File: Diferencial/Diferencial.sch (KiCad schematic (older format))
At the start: 68 parts, among them J1 Pedal Sensor 1, J2 Pedal Sensor 2, J3 DB9_Female, J4 DB9_Female, J5 Screw_Terminal_01x02, J6 Brake Sensor, J7 Out_Brake_Light, K1 RELAY_19.1x15.5mm, Q1 BC547, Q2 BC547, U1 LM358, U2 LM358, U3 MCP2558FD-xSN, U4 LM317_TO39, U5 UFRGS_PILL

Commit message: Diferencial Update
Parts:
- added C14: 100n, Capacitor_SMD:C_0805_2012Metric_Pad1.15x1.40mm_HandSolder, symbol Device:C
- added C15: 1u, Capacitor_SMD:C_0805_2012Metric_Pad1.15x1.40mm_HandSolder, symbol Device:C
- added D7: LED, e-Power:LED_0805_1.15x1.40mm_HandSolder, symbol Device:LED
- added J8: Brake Sensor 2, Connector_Phoenix_GMSTB:PhoenixContact_GMSTBA_2,5_3-G_1x03_P7.50mm_Horizontal, symbol Connector_Generic:Conn_01x03
- added R33, R36: ADJ, Resistor_SMD:R_0805_2012Metric_Pad1.15x1.40mm_HandSolder, symbol Device:R
- added R34: 2K7, Resistor_SMD:R_0805_2012Metric_Pad1.15x1.40mm_HandSolder, symbol Device:R
- added R35: 2K2, Resistor_SMD:R_0805_2012Metric_Pad1.15x1.40mm_HandSolder, symbol Device:R
- added R37: 3K3, Resistor_SMD:R_0805_2012Metric_Pad1.15x1.40mm_HandSolder, symbol Device:R
- added R38, R39, R40: 10K, Resistor_SMD:R_0805_2012Metric_Pad1.15x1.40mm_HandSolder, symbol Device:R
- added R41: 330, Resistor_SMD:R_0805_2012Metric_Pad1.15x1.40mm_HandSolder, symbol Device:R
- added unit 2 of U2
- J6: value Brake Sensor -> Brake Sensor 1
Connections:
- net labels added: Brake_Sensor_1, Brake_Sensor_2
- net labels removed: Brake_Sensor, PA5, PA6, PA7, Steering_Wheel
- wire segments 130 -> 160
- no-connect marks 30 -> 29
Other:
- note added: "Acceleration Pedal"
- note added: "Brake Light Signal"
- note added: "Brake Pedal"
- note added: "CAN"
- note added: "Input Filter"
- note added: "Ready to Drive"
- moved on the sheet: C10, C11, C12, C13, C2, C3, C5, C6, C7, C8, C9, D2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

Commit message: Diferencial Layout Update/Main ECU Eeschema
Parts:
- removed D1: D_SCH_1N5819, Diode_SMD:D_SOD-323_HandSoldering, symbol e-Power:D_SCH_1N5819
- removed D5: 1N4148, e-Power:DO-35_SMD, symbol Diode:1N4148
- removed Q1: BC547, Package_TO_SOT_SMD:SC-59_Handsoldering, symbol Transistor_BJT:BC547
- removed Q2: BC547, e-Power:SOT-23, symbol Transistor_BJT:BC547
- removed R10, R36: ADJ, Resistor_SMD:R_0805_2012Metric_Pad1.15x1.40mm_HandSolder, symbol Device:R
- removed R11: 2K2, Resistor_SMD:R_0805_2012Metric_Pad1.15x1.40mm_HandSolder, symbol Device:R
- removed R2: 1K2, Resistor_SMD:R_0805_2012Metric_Pad1.15x1.40mm_HandSolder, symbol Device:R
- removed R22, R23, R24: 330, Resistor_SMD:R_0805_2012Metric_Pad1.15x1.40mm_HandSolder, symbol Device:R
- removed R34: 2K7, Resistor_SMD:R_0805_2012Metric_Pad1.15x1.40mm_HandSolder, symbol Device:R
- added D5, D6: D_SCH_SS54HF, e-Power:DO-214AC, symbol e-Power:D_SCH_SS54HF
- added G1: Logo_UFRGS_Large, e-Power:Logo_UFRGS_14.7x8.0mm_SilkS, symbol e-Power:Logo_UFRGS_Large
- added G2: Logo_e-Power_Large, e-Power:Logo_e-Power_16.5x8.0mm_SilkS, symbol e-Power:Logo_e-Power_Large
- added H1: +12V, e-Power:MountingHole_3.2mm_M3_Pad_Via, symbol Mechanical:MountingHole_Pad
- added H2, H3, H4: GND, e-Power:MountingHole_3.2mm_M3_Pad_Via, symbol Mechanical:MountingHole_Pad
- added Q1, Q2: MMBT3904, Package_TO_SOT_SMD:SOT-23, symbol Transistor_BJT:MMBT3904
- added R15, R20, R31, R32, R43, R44, R50, R51, R52, R57, R8: 1K, Resistor_SMD:R_0805_2012Metric_Pad1.15x1.40mm_HandSolder, symbol Device:R
- added R16, R17, R26, R27, R29, R38, R39, R4, R40, R41, R7: 10K, Resistor_SMD:R_0805_2012Metric_Pad1.15x1.40mm_HandSolder, symbol Device:R
- added R46, R48: 10R, Resistor_SMD:R_0805_2012Metric_Pad1.15x1.40mm_HandSolder, symbol Device:R
- added TP1: 12V, e-Power:TestPoint_Pad_D1.0mm, symbol Connector:TestPoint
- added TP2: 5V, e-Power:TestPoint_Pad_D1.0mm, symbol Connector:TestPoint
- added TP? (x7): GND, e-Power:TestPoint_Pad_D1.0mm, symbol Connector:TestPoint
- C14: renamed from C12; value 470u -> 220u
- C15: renamed from C13; value 470u -> 220u
- F1: footprint Fuse:Fuse_0805_2012Metric_Pad1.15x1.40mm_HandSolder -> e-Power:FUSE_1206_3216Metric
- FB1: footprint e-Power:FB_0603_1608Metric -> e-Power:FB_0805_2012Metric
- J1, J2: footprint Connector_Phoenix_GMSTB:PhoenixContact_GMSTBA_2,5_3-G_1x03_P7.50mm_Horizontal -> e-Power:TerminalBlock_Phoenix_MKDS-1,5-4-5.08_1x04_P5.08mm_Horizontal
- J3: renamed from J6; footprint Connector_Phoenix_GMSTB:PhoenixContact_GMSTBA_2,5_3-G_1x03_P7.50mm_Horizontal -> e-Power:TerminalBlock_Phoenix_MKDS-1,5-4-5.08_1x04_P5.08mm_Horizontal
- J4: renamed from J8; footprint Connector_Phoenix_GMSTB:PhoenixContact_GMSTBA_2,5_3-G_1x03_P7.50mm_Horizontal -> e-Power:TerminalBlock_Phoenix_MKDS-1,5-4-5.08_1x04_P5.08mm_Horizontal
- J5: renamed from J7; footprint Connector_Phoenix_GMSTB:PhoenixContact_GMSTBA_2,5_2-G-7,62_1x02_P7.62mm_Horizontal -> e-Power:TerminalBlock_Phoenix_MKDS-1,5-2_1x02_P5.08mm_Horizontal
- J6: renamed from J5; value Screw_Terminal_01x02 -> Buzzer_out; footprint Connector_Phoenix_GMSTB:PhoenixContact_GMSTBA_2,5_2-G-7,62_1x02_P7.62mm_Horizontal -> e-Power:TerminalBlock_Phoenix_MKDS-1,5-2_1x02_P5.08mm_Horizontal
- R13, R28: value 2K2 -> 10K
- R14, R21: value 330 -> 1K
- R18: value 2K7 -> 1K
- R22: renamed from R41; value 330 -> 1K
- R3: value 18K -> ADJ
- R30, R37: value 3K3 -> 10K
- R35: value 2K2 -> ADJ
- R49: renamed from R19; value 120 -> 100R
- R5: value 1K2 -> 1K
- R6: value 18K -> 10K
- U1: footprint e-Power:DIP-8_SMD -> Package_SO:SOIC-8_3.9x4.9mm_P1.27mm
- U3: renamed from U2; footprint e-Power:DIP-8_SMD -> Package_SO:SOIC-8_3.9x4.9mm_P1.27mm
- U5: renamed from U4; footprint Package_TO_SOT_THT:TO-39-3 -> e-Power:TO-220-3_Horizontal_TabDown
- renumbered C15 to C10, C10 to C11, C9 to C12, C11 to C13, C4 to C2, C7 to C3, C2 to C4, C3 to C6, C6 to C7, C14 to C9, D2 to D1, D3 to D2, D4 to D3, D7 to D4, D6 to D7, J3 to J7, J4 to J8, R17 to R10, R12 to R11, R7 to R12, R8 to R19, R16 to R2, R15 to R23, R31 to R24, R29 to R25, R38 to R34, R39 to R36, R40 to R42, R32 to R45, R20 to R47, R26 to R53, R25 to R54, R27 to R55, R9 to R56, R4 to R9, U5 to U2, U2 to U3, U3 to U4
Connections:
- wire segments 160 -> 202
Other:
- moved on the sheet: J1, J2, J3, J4, R23, R25, R49, R53, R9

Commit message: Diferencial Layout Update
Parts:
- removed J7: DB9_Female, e-Power:DSUB-9_Female_EdgeMount_P2.77mm, symbol Connector:DB9_Female
- removed U5: LM317_TO39, e-Power:TO-220-3_Horizontal_TabDown, symbol Regulator_Linear:LM317_TO39
- added J7: Screw_Terminal_01x04, e-Power:TerminalBlock_Phoenix_MKDS-1,5-4-5.08_1x04_P5.08mm_Horizontal, symbol Connector:Screw_Terminal_01x04
- added U5: LM317_3PinPackage, e-Power:TO-220-3_Horizontal_TabDown, symbol Regulator_Linear:LM317_3PinPackage
- TP3: renamed from TP?; value GND -> AS_1
- TP4: renamed from TP?; value GND -> AS_2
- TP6: renamed from TP?; value GND -> BS_1
- TP7: renamed from TP?; value GND -> BS_2
- gave numbers to parts that had none: 3
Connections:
- net +12V: now also U5.3 (VI)
- net +5V: now also U5.2 (VO)
- net Brake_Light: now also U2.25 (PA1); no longer U2.10 (PA9)
- net Brake_Sensor_1: now also U2.10 (PA9); no longer U2.25 (PA1)
- net Brake_Sensor_2: now also U2.9 (PA8); no longer U2.24 (PA0)
- net CAN_H: now also J7.3 (Pin_3)
- net CAN_L: now also J7.2 (Pin_2)
- net GND: now also J7.1 (Pin_1)
- net Input_Power: now also J7.4 (Pin_4)
- net Ready_to_Drive: now also U2.24 (PA0); no longer U2.9 (PA8)
- net at R50.2, R51.2, R52.2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: now also U5.1 (ADJ)
- no-connect marks 29 -> 27
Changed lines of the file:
@@
-	1    0    0    -1
-$EndComp
-$Comp
-L Regulator_Linear:LM317_TO39 U5
-U 1 1 5ECB47C0
-P 14475 8525
-F 0 "U5" H 14475 8767 50  0000 C CNN
-F 1 "LM317_TO39" H 14475 8676 50  0000 C CNN
-F 2 "e-Power:TO-220-3_Horizontal_TabDown" H 14475 8750 50  0001 C CIN
-F 3 "http://www.ti.com/lit/ds/symlink/lm317.pdf" H 14475 8525 50  0001 C CNN
-	1    14475 8525
 	1    0    0    -1
 $EndComp
@@
 	1    0    0    -1
 $EndComp
-$Comp
-L Connector:DB9_Female J7
-U 1 1 5ED2A193
-P 1550 9900
-F 0 "J7" H 1730 9946 50  0000 L CNN
-F 1 "DB9_Female" H 1730 9855 50  0000 L CNN
-F 2 "e-Power:DSUB-9_Female_EdgeMount_P2.77mm" H 1550 9900 50  0001 C CNN
-F 3 " ~" H 1550 9900 50  0001 C CNN
-	1    1550 9900
-	-1   0    0    1
-$EndComp
-$Comp
-L power:GND #PWR054
-U 1 1 5ED2A199
-P 1850 10200
-F 0 "#PWR054" H 1850 9950 50  0001 C CNN
-F 1 "GND" V 1855 10072 50  0000 R CNN
-F 2 "" H 1850 10200 50  0001 C CNN
-F 3 "" H 1850 10200 50  0001 C CNN
-	1    1850 10200
-	0    -1   -1   0
-$EndComp
-$Comp
-L power:GND #PWR048
-U 1 1 5ED2A19F
-P 1850 9500
-F 0 "#PWR048" H 1850 9250 50  0001 C CNN
-F 1 "GND" V 1855 9372 50  0000 R CNN
-F 2 "" H 1850 9500 50  0001 C CNN
-F 3 "" H 1850 9500 50  0001 C CNN
-	1    1850 9500
-	0    -1   -1   0
-$EndComp
-Wire Wire Line
-	1850 9600 2425 9600
-Text Label 2425 9600 2    50   ~ 0
+Wire Wire Line
+	1725 9775 2300 9775
+Text Label 2300 9775 2    50   ~ 0
+CAN_H
+Wire Wire Line
+	1725 9875 2300 9875
+Text Label 2300 9875 2    50   ~ 0
+CAN_L
+Wire Wire Line
+	1725 9975 2300 9975
+Text Label 2300 9975 2    50   ~ 0
+CAN_GND
+Wire Wire Line
+	1725 9675 2300 9675
+Text Label 2300 9675 2    50   ~ 0
 Input_Power
-Wire Wire Line
-	1850 10000 2425 10000
-Text Label 2425 10000 2    50   ~ 0
-CAN_H
-Wire Wire Line
-	1850 10100 2425 10100
-Text Label 2425 10100 2    50   ~ 0
-CAN_L
-Wire Wire Line
-	1850 9900 2425 9900
-Text Label 2425 9900 2    50   ~ 0
-CAN_GND
-Wire Wire Line
-	1850 10300 2425 10300
-Text Label 2425 10300 2    50   ~ 0
-Input_Power
-NoConn ~ 1850 9700
-NoConn ~ 1850 9800
-Text Label 10500 2925 2    50   ~ 0
+Text Label 11550 3725 0    50   ~ 0
 Ready_to_Drive
 Text Label 6475 9325 2    50   ~ 0
@@
 $EndComp
 NoConn ~ 8825 8500
-Text Label 11550 3625 0    50   ~ 0
+Text Label 10500 3025 2    50   ~ 0
 Brake_Sensor_1
 Connection ~ 4000 2450
@@
 	1    0    0    -1
 $EndComp
-Wire Wire Line
-	4925 4175 4950 4175
 Connection ~ 4925 4175
 $Comp
@@
 	-1   0    0    1
 $EndComp
-Text Label 5175 4175 0    50   ~ 0
-Brake_Sensor_1
 Connection ~ 4425 4175
 Wire Wire Line
@@
 Text Label 15125 7325 0    50   ~ 0
 Brake_Light
-Text Label 10500 3025 2    50   ~ 0
+Text Label 11550 3625 0    50   ~ 0
 Brake_Light
-Text Label 11550 3725 0    50   ~ 0
+Text Label 10500 2925 2    50   ~ 0
 Brake_Sensor_2
 Wire Notes Line
@@
 $EndComp
 $Comp
-L Connector:TestPoint TP?
+L Connector:TestPoint TP9
 U 1 1 5F3C7037
 P 14975 9450
-F 0 "TP?" H 14900 9725 50  0000 L CNN
+F 0 "TP9" H 14900 9725 50  0000 L CNN
 F 1 "GND" H 14900 9650 50  0000 L CNN
 F 2 "e-Power:TestPoint_Pad_D1.0mm" H 15175 9450 50  0001 C CNN
@@
 	14975 9450 14975 9500
 $Comp
-L Connector:TestPoint TP?
+L Connector:TestPoint TP3
 U 1 1 5F3C983B
 P 4925 1050
-F 0 "TP?" H 4850 1325 50  0000 L CNN
-F 1 "GND" H 4850 1250 50  0000 L CNN
+F 0 "TP3" H 4850 1325 50  0000 L CNN
+F 1 "AS_1" H 4850 1250 50  0000 L CNN
 F 2 "e-Power:TestPoint_Pad_D1.0mm" H 5125 1050 50  0001 C CNN
 F 3 "~" H 5125 1050 50  0001 C CNN
@@
 $EndComp
 $Comp
-L Connector:TestPoint TP?
+L Connector:TestPoint TP4
 U 1 1 5F3CA5F4
 P 4900 2450
-F 0 "TP?" H 4825 2725 50  0000 L CNN
-F 1 "GND" H 4825 2650 50  0000 L CNN
+F 0 "TP4" H 4825 2725 50  0000 L CNN
+F 1 "AS_2" H 4825 2650 50  0000 L CNN
 F 2 "e-Power:TestPoint_Pad_D1.0mm" H 5100 2450 50  0001 C CNN
 F 3 "~" H 5100 2450 50  0001 C CNN
@@
 $EndComp
 $Comp
-L Connector:TestPoint TP?
+L Connector:TestPoint TP7
 U 1 1 5F3CAABA
 P 4925 5675
-F 0 "TP?" H 4850 5950 50  0000 L CNN
-F 1 "GND" H 4850 5875 50  0000 L CNN
+F 0 "TP7" H 4850 5950 50  0000 L CNN
+F 1 "BS_2" H 4850 5875 50  0000 L CNN
 F 2 "e-Power:TestPoint_Pad_D1.0mm" H 5125 5675 50  0001 C CNN
 F 3 "~" H 5125 5675 50  0001 C CNN
@@
 	1    0    0    -1
 $EndComp
-Connection ~ 4950 4175
-Wire Wire Line
-	4950 4175 5175 4175
-$Comp
-L Connector:TestPoint TP?
+$Comp
+L Connector:TestPoint TP6
 U 1 1 5F3CB025
 P 4925 4175
-F 0 "TP?" H 4850 4450 50  0000 L CNN
-F 1 "GND" H 4850 4375 50  0000 L CNN
+F 0 "TP6" H 4850 4450 50  0000 L CNN
+F 1 "BS_1" H 4850 4375 50  0000 L CNN
 F 2 "e-Power:TestPoint_Pad_D1.0mm" H 5125 4175 50  0001 C CNN
 F 3 "~" H 5125 4175 50  0001 C CNN
@@
 $EndComp
 $Comp
-L Connector:TestPoint TP?
+L Connector:TestPoint TP8
 U 1 1 5F3CB6F0
 P 5475 6350
-F 0 "TP?" H 5400 6625 50  0000 L CNN
+F 0 "TP8" H 5400 6625 50  0000 L CNN
 F 1 "GND" H 5400 6550 50  0000 L CNN
 F 2 "e-Power:TestPoint_Pad_D1.0mm" H 5675 6350 50  0001 C CNN
@@
 $EndComp
 $Comp
-L Connector:TestPoint TP?
+L Connector:TestPoint TP5
 U 1 1 5F3CBF2E
 P 5475 3125
-F 0 "TP?" H 5400 3400 50  0000 L CNN
+F 0 "TP5" H 5400 3400 50  0000 L CNN
 F 1 "GND" H 5400 3325 50  0000 L CNN
 F 2 "e-Power:TestPoint_Pad_D1.0mm" H 5675 3125 50  0001 C CNN
@@
 Connection ~ 5475 3125
 Connection ~ 5475 6350
+Wire Wire Line
+	4925 4175 5175 4175
+$Comp
+L Regulator_Linear:LM317_3PinPackage U5
+U 1 1 5F3B31FD
+P 14475 8525
+F 0 "U5" H 14475 8767 50  0000 C CNN
+F 1 "LM317_3PinPackage" H 14475 8676 50  0000 C CNN
+F 2 "e-Power:TO-220-3_Horizontal_TabDown" H 14475 8775 50  0001 C CIN
+F 3 "http://www.ti.com/lit/ds/symlink/lm317.pdf" H 14475 8525 50  0001 C CNN
+	1    14475 8525
+	1    0    0    -1
+$EndComp
+Text Label 5175 4175 0    50   ~ 0
+Brake_Sensor_1
+$Comp
+L Connector:Screw_Terminal_01x04 J7
+U 1 1 5F83DA47
+P 1525 9875
+F 0 "J7" H 1443 9450 50  0000 C CNN
+F 1 "Screw_Terminal_01x04" H 1443 9541 50  0000 C CNN
+F 2 "e-Power:TerminalBlock_Phoenix_MKDS-1,5-4-5.08_1x04_P5.08mm_Horizontal" H 1525 9875 50  0001 C CNN
+F 3 "~" H 1525 9875 50  0001 C CNN
+	1    1525 9875
+	-1   0    0    1
+$EndComp
 $EndSCHEMATC

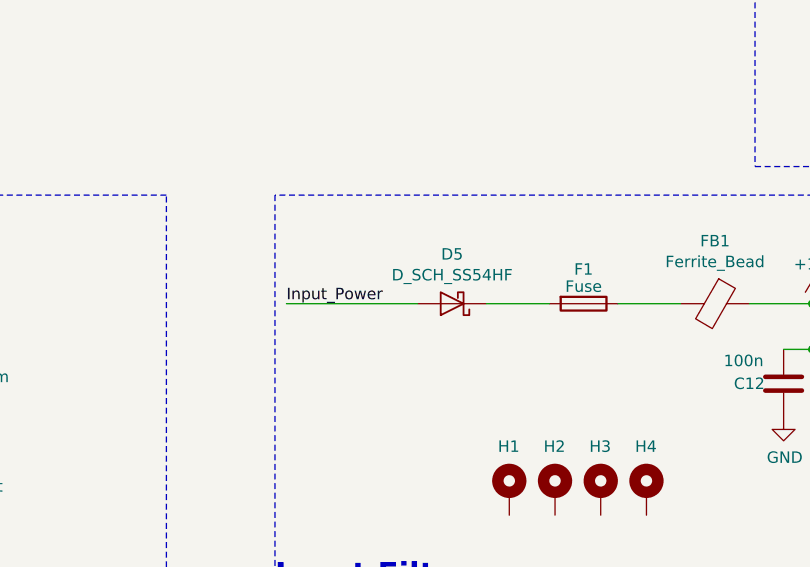
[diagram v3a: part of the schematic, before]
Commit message: Layout Fixes and CAN Connector Added
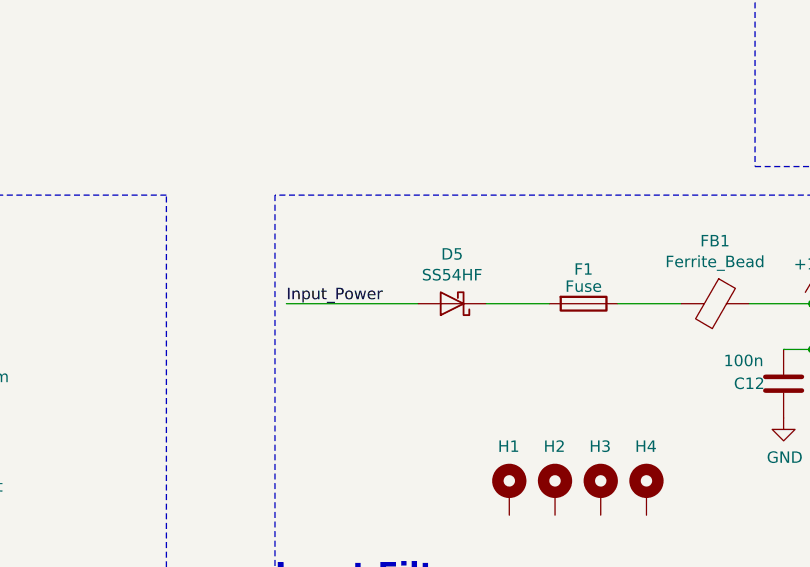
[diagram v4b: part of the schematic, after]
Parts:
- removed D5: D_SCH_SS54HF, e-Power:DO-214AC, symbol e-Power:D_SCH_SS54HF
- added D5: SS54HF, e-Power:DO-214AC, symbol e-Power:SS54HF
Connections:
- net Input_Power: now also D5.2 (A)
- net at F1.2: now also D5.1 (K)
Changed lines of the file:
@@
 NoConn ~ 4200 10100
 NoConn ~ 4200 10000
-Wire Wire Line
-	11675 8525 11100 8525
 Text Label 11100 8525 0    50   ~ 0
 Input_Power
@@
 	12850 2775 12850 3025
 $Comp
-L e-Power:D_SCH_SS54HF D5
-U 1 1 5F30CB96
-P 11825 8525
-F 0 "D5" H 11825 8309 50  0000 C CNN
-F 1 "D_SCH_SS54HF" H 11825 8400 50  0000 C CNN
-F 2 "e-Power:DO-214AC" H 11825 8350 50  0001 C CNN
-F 3 "https://br.mouser.com/datasheet/2/80/20190806165140-1729178.pdf" H 11700 8600 50  0001 C CNN
-F 4 "C22452" H 11825 8625 50  0001 C CNN "LCSC"
-	1    11825 8525
-	-1   0    0    1
-$EndComp
-$Comp
 L Connector:TestPoint TP1
 U 1 1 5F313597
@@
 	-1   0    0    1
 $EndComp
+$Comp
+L e-Power:SS54HF D5
+U 1 1 5F4E4A0E
+P 11825 8525
+F 0 "D5" H 11825 8309 50  0000 C CNN
+F 1 "SS54HF" H 11825 8400 50  0000 C CNN
+F 2 "e-Power:DO-214AC" H 11825 8350 50  0001 C CNN
+F 3 "" H 11825 8525 50  0001 C CNN
+	1    11825 8525
+	-1   0    0    1
+$EndComp
+Wire Wire Line
+	11100 8525 11675 8525
 $EndSCHEMATC

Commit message: Added CAN connectors / Fixes
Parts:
- removed J8: DB9_Female, e-Power:DSUB-9_Female_EdgeMount_P2.77mm, symbol Connector:DB9_Female
- removed R36, R42: 10K, Resistor_SMD:R_0805_2012Metric_Pad1.15x1.40mm_HandSolder, symbol Device:R
- removed TP8: GND, e-Power:TestPoint_Pad_D1.0mm, symbol Connector:TestPoint
- added J8: CAN_1, e-Power:Molex_Mini-Fit_Jr_2x04_P4.20mm_Horizontal, symbol Connector:Screw_Terminal_01x08
- C14, C15: footprint Capacitor_SMD:CP_Elec_8x10 -> Capacitor_SMD:CP_Elec_10x10
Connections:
- net Brake_Sensor_2: now also C10.2, C9.2, R34.2, TP7.1
- net CAN_H: now also J8.4 (Pin_4)
- net CAN_L: now also J8.3 (Pin_3)
- net GND: now also J8.2 (Pin_2), J8.5 (Pin_5), J8.8 (Pin_8)
- net Input_Power: now also J8.1 (Pin_1), J8.7 (Pin_7)
- no-connect marks 27 -> 26
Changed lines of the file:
@@
-$EndComp
-$Comp
-L Connector:DB9_Female J8
-U 1 1 5ECE338B
-P 4500 9900
-F 0 "J8" H 4680 9946 50  0000 L CNN
-F 1 "DB9_Female" H 4680 9855 50  0000 L CNN
-F 2 "e-Power:DSUB-9_Female_EdgeMount_P2.77mm" H 4500 9900 50  0001 C CNN
-F 3 " ~" H 4500 9900 50  0001 C CNN
-	1    4500 9900
-	1    0    0    -1
 $EndComp
 $Comp
 L power:GND #PWR051
 U 1 1 5ECE6E6B
-P 4200 9600
-F 0 "#PWR051" H 4200 9350 50  0001 C CNN
-F 1 "GND" V 4205 9472 50  0000 R CNN
-F 2 "" H 4200 9600 50  0001 C CNN
-F 3 "" H 4200 9600 50  0001 C CNN
-	1    4200 9600
+P 4675 9600
+F 0 "#PWR051" H 4675 9350 50  0001 C CNN
+F 1 "GND" V 4680 9472 50  0000 R CNN
+F 2 "" H 4675 9600 50  0001 C CNN
+F 3 "" H 4675 9600 50  0001 C CNN
+	1    4675 9600
 	0    1    1    0
 $EndComp
@@
 L power:GND #PWR055
 U 1 1 5ECE7C93
-P 4200 10300
-F 0 "#PWR055" H 4200 10050 50  0001 C CNN
-F 1 "GND" V 4205 10172 50  0000 R CNN
-F 2 "" H 4200 10300 50  0001 C CNN
-F 3 "" H 4200 10300 50  0001 C CNN
-	1    4200 10300
-	0    1    1    0
-$EndComp
-Wire Wire Line
-	4200 10200 3625 10200
-Text Label 3625 10200 0    50   ~ 0
+P 4675 10200
+F 0 "#PWR055" H 4675 9950 50  0001 C CNN
+F 1 "GND" V 4680 10072 50  0000 R CNN
+F 2 "" H 4675 10200 50  0001 C CNN
+F 3 "" H 4675 10200 50  0001 C CNN
+	1    4675 10200
+	0    1    1    0
+$EndComp
+Wire Wire Line
+	4675 10100 4100 10100
+Text Label 4100 10100 0    50   ~ 0
 Input_Power
 Wire Wire Line
-	4200 9800 3625 9800
-Text Label 3625 9800 0    50   ~ 0
+	4675 9800 4100 9800
+Text Label 4100 9800 0    50   ~ 0
 CAN_H
 Wire Wire Line
-	4200 9700 3625 9700
-Text Label 3625 9700 0    50   ~ 0
+	4675 9700 4100 9700
+Text Label 4100 9700 0    50   ~ 0
 CAN_L
 Wire Wire Line
-	4200 9900 3625 9900
-Text Label 3625 9900 0    50   ~ 0
+	4675 9900 4100 9900
+Text Label 4100 9900 0    50   ~ 0
 CAN_GND
 Wire Wire Line
-	4200 9500 3625 9500
-Text Label 3625 9500 0    50   ~ 0
+	4675 9500 4100 9500
+Text Label 4100 9500 0    50   ~ 0
 Input_Power
-NoConn ~ 4200 10100
-NoConn ~ 4200 10000
+NoConn ~ 4675 10000
 Text Label 11100 8525 0    50   ~ 0
 Input_Power
@@
 F 0 "C14" H 14100 8850 50  0000 L CNN
 F 1 "220u" H 14100 8925 50  0000 L CNN
-F 2 "Capacitor_SMD:CP_Elec_8x10" H 14038 8725 50  0001 C CNN
+F 2 "Capacitor_SMD:CP_Elec_10x10" H 14038 8725 50  0001 C CNN
 F 3 "~" H 14000 8875 50  0001 C CNN
 	1    14000 8875
@@
 F 0 "C15" H 15650 8825 50  0000 L CNN
 F 1 "220u" H 15650 8900 50  0000 L CNN
-F 2 "Capacitor_SMD:CP_Elec_8x10" H 15563 8725 50  0001 C CNN
+F 2 "Capacitor_SMD:CP_Elec_10x10" H 15563 8725 50  0001 C CNN
 F 3 "~" H 15525 8875 50  0001 C CNN
 	1    15525 8875
@@
 	-1   0    0    1
 $EndComp
-Text Label 5475 6025 0    50   ~ 0
+Text Label 5175 5675 0    50   ~ 0
 Brake_Sensor_2
 Connection ~ 4425 5675
@@
 	650  6625 6850 6625
 $Comp
-L Device:R R36
-U 1 1 5F54635D
-P 5475 5825
-F 0 "R36" V 5550 5750 50  0000 L CNN
-F 1 "10K" V 5475 5750 50  0000 L CNN
-F 2 "Resistor_SMD:R_0805_2012Metric_Pad1.15x1.40mm_HandSolder" V 5405 5825 50  0001 C CNN
-F 3 "~" H 5475 5825 50  0001 C CNN
-	1    5475 5825
-	-1   0    0    1
-$EndComp
-$Comp
-L Device:R R42
-U 1 1 5F546363
-P 5475 6200
-F 0 "R42" V 5550 6125 50  0000 L CNN
-F 1 "10K" V 5475 6125 50  0000 L CNN
-F 2 "Resistor_SMD:R_0805_2012Metric_Pad1.15x1.40mm_HandSolder" V 5405 6200 50  0001 C CNN
-F 3 "~" H 5475 6200 50  0001 C CNN
-	1    5475 6200
-	-1   0    0    1
-$EndComp
-Wire Wire Line
-	5475 5975 5475 6050
-$Comp
-L power:GND #PWR033
-U 1 1 5F54636A
-P 5475 6350
-F 0 "#PWR033" H 5475 6100 50  0001 C CNN
-F 1 "GND" H 5480 6177 50  0000 C CNN
-F 2 "" H 5475 6350 50  0001 C CNN
-F 3 "" H 5475 6350 50  0001 C CNN
-	1    5475 6350
-	1    0    0    -1
-$EndComp
-Wire Wire Line
-	4925 5675 5475 5675
-$Comp
 L power:GND #PWR020
 U 1 1 5F56AC93
@@
 $EndComp
 $Comp
-L Connector:TestPoint TP8
-U 1 1 5F3CB6F0
-P 5475 6350
-F 0 "TP8" H 5400 6625 50  0000 L CNN
-F 1 "GND" H 5400 6550 50  0000 L CNN
-F 2 "e-Power:TestPoint_Pad_D1.0mm" H 5675 6350 50  0001 C CNN
-F 3 "~" H 5675 6350 50  0001 C CNN
-	1    5475 6350
-	0    1    1    0
-$EndComp
-$Comp
 L Connector:TestPoint TP5
 U 1 1 5F3CBF2E
@@
 $EndComp
 Connection ~ 5475 3125
-Connection ~ 5475 6350
 Wire Wire Line
 	4925 4175 5175 4175
@@
 Wire Wire Line
 	11100 8525 11675 8525
+Wire Wire Line
+	4925 5675 5175 5675
+$Comp
+L Connector:Screw_Terminal_01x08 J8
+U 1 1 5F6109CB
+P 4875 9800
+F 0 "J8" H 4955 9792 50  0000 L CNN
+F 1 "CAN_1" H 4955 9701 50  0000 L CNN
+F 2 "e-Power:Molex_Mini-Fit_Jr_2x04_P4.20mm_Horizontal" H 4875 9800 50  0001 C CNN
+F 3 "~" H 4875 9800 50  0001 C CNN
+	1    4875 9800
+	1    0    0    -1
+$EndComp
 $EndSCHEMATC
